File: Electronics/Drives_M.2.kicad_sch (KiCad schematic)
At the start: 87 parts, among them IC3 LM61480Q3RPHRQ1, J16 Bus_M.2_Socket_M, J17 Bus_M.2_Socket_M, J18 Bus_M.2_Socket_M, J19 Bus_M.2_Socket_M, M1 M.2 Screw, M10 M.2 Solder Nut, M11 M.2 Screw, M12 M.2 Screw, M13 M.2 Solder Nut, M14 M.2 Solder Nut, M15 M.2 Solder Nut, M16 M.2 Solder Nut, M17 M.2 Solder Nut, M18 M.2 Solder Nut, M19 M.2 Solder Nut, M2 M.2 Screw, M20 M.2 Solder Nut, M3 M.2 Solder Nut, M4 M.2 Solder Nut, M5 M.2 Solder Nut, M6 M.2 Solder Nut, M7 M.2 Solder Nut, M8 M.2 Solder Nut, M9 M.2 Solder Nut, U7 ASEK-32.768KHZ-L-R-T, U8 ASM1184

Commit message: Changed sata port
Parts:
- C58: renamed from C54; footprint Capacitor_SMD:C_0603_1608Metric -> Capacitor_SMD:C_0402_1005Metric
- C59: renamed from C55; footprint Capacitor_SMD:C_0603_1608Metric -> Capacitor_SMD:C_0402_1005Metric
- C60: renamed from C56; footprint Capacitor_SMD:C_0603_1608Metric -> Capacitor_SMD:C_0402_1005Metric
- C61: renamed from C57; footprint Capacitor_SMD:C_0603_1608Metric -> Capacitor_SMD:C_0402_1005Metric
- C62: renamed from C58; footprint Capacitor_SMD:C_0603_1608Metric -> Capacitor_SMD:C_0402_1005Metric
- C63: renamed from C59; footprint Capacitor_SMD:C_0603_1608Metric -> Capacitor_SMD:C_0402_1005Metric
- C69: renamed from C65; footprint Capacitor_SMD:C_0603_1608Metric -> Capacitor_SMD:C_0402_1005Metric
- C70: renamed from C66; footprint Capacitor_SMD:C_0603_1608Metric -> Capacitor_SMD:C_0402_1005Metric
- C71: renamed from C67; footprint Capacitor_SMD:C_0603_1608Metric -> Capacitor_SMD:C_0402_1005Metric
- C72: renamed from C68; footprint Capacitor_SMD:C_0603_1608Metric -> Capacitor_SMD:C_0402_1005Metric
- C73: renamed from C69; footprint Capacitor_SMD:C_0603_1608Metric -> Capacitor_SMD:C_0402_1005Metric
- C74: renamed from C70; footprint Capacitor_SMD:C_0603_1608Metric -> Capacitor_SMD:C_0402_1005Metric
- C82: renamed from C78; footprint Capacitor_SMD:C_0603_1608Metric -> Capacitor_SMD:C_0402_1005Metric
- C83: renamed from C79; footprint Capacitor_SMD:C_0603_1608Metric -> Capacitor_SMD:C_0402_1005Metric
- C84: renamed from C80; footprint Capacitor_SMD:C_0603_1608Metric -> Capacitor_SMD:C_0402_1005Metric
- C85: renamed from C81; footprint Capacitor_SMD:C_0603_1608Metric -> Capacitor_SMD:C_0402_1005Metric
- C86: renamed from C82; footprint Capacitor_SMD:C_0603_1608Metric -> Capacitor_SMD:C_0402_1005Metric
- C87: renamed from C83; footprint Capacitor_SMD:C_0603_1608Metric -> Capacitor_SMD:C_0402_1005Metric
- J16: renamed from J18; footprint M.2 M Key socket:M.2 M Key socket -> M.2 M Key socket:M.2 M Key socket WN HOLES
- J17: renamed from J19; footprint M.2 M Key socket:M.2 M Key socket -> M.2 M Key socket:M.2 M Key socket WN HOLES
- U8: footprint Package_DFN_QFN:QFN-64-1EP_9x9mm_P0.5mm_EP5.2x5.2mm -> Package_DFN_QFN:QFN-64-1EP_9x9mm_P0.5mm_EP5.2x5.2mm_ThermalVias
- renumbered C52 to C56, C53 to C57, C60 to C64, C61 to C65, C62 to C66, C63 to C67, C64 to C68, C71 to C75, C72 to C76, C73 to C77, C74 to C78, C75 to C79, C76 to C80, C77 to C81, C84 to C88, C85 to C89, C86 to C90, C87 to C91, C88 to C92, C89 to C93, J16 to J14, J17 to J15, R32 to R30, R33 to R31, R34 to R32, R35 to R33, R36 to R34, R37 to R35, R38 to R36, R39 to R37, R40 to R38, R41 to R39, R42 to R40, R43 to R41, R44 to R42, R45 to R43, R46 to R44, R47 to R45, TP12 to TP9

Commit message: More pcbing
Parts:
- removed TP9: TestPoint, TestPoint:TestPoint_Pad_1.0x1.0mm, symbol Connector:TestPoint
- added C94: 47u, Capacitor_SMD:C_0805_2012Metric, symbol Device:C_Small
- J16, J17: footprint M.2 M Key socket:M.2 M Key socket WN HOLES -> M.2 M Key socket:M.2 M Key socket
- R35: footprint Resistor_SMD:R_0603_1608Metric -> Resistor_SMD:R_0402_1005Metric
- renumbered C91 to C90, C92 to C91, C93 to C92, C90 to C93
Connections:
- net BOOT: now also IC3.16 (SW), L5.1
- net PCIe_CLK_N_3: now also J15.53 (REFCLKn)
- net PCIe_CLK_N_4: no longer J15.53 (REFCLKn)
- net PCIe_CLK_P_3: now also J15.55 (REFCLKp)
- net PCIe_CLK_P_4: no longer J15.55 (REFCLKp)
- net gnd: now also C94.2
- net TX_P_3: now reaches C67.2, U8.39 (TXP_3)
- net TX_N_3: now reaches C68.2, U8.40 (TXN_3)
- net FB renamed +3V3 M.2
- net +3V3 M.2: now also C94.1
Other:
- moved on the sheet: C67, C68, C91, C92, C93

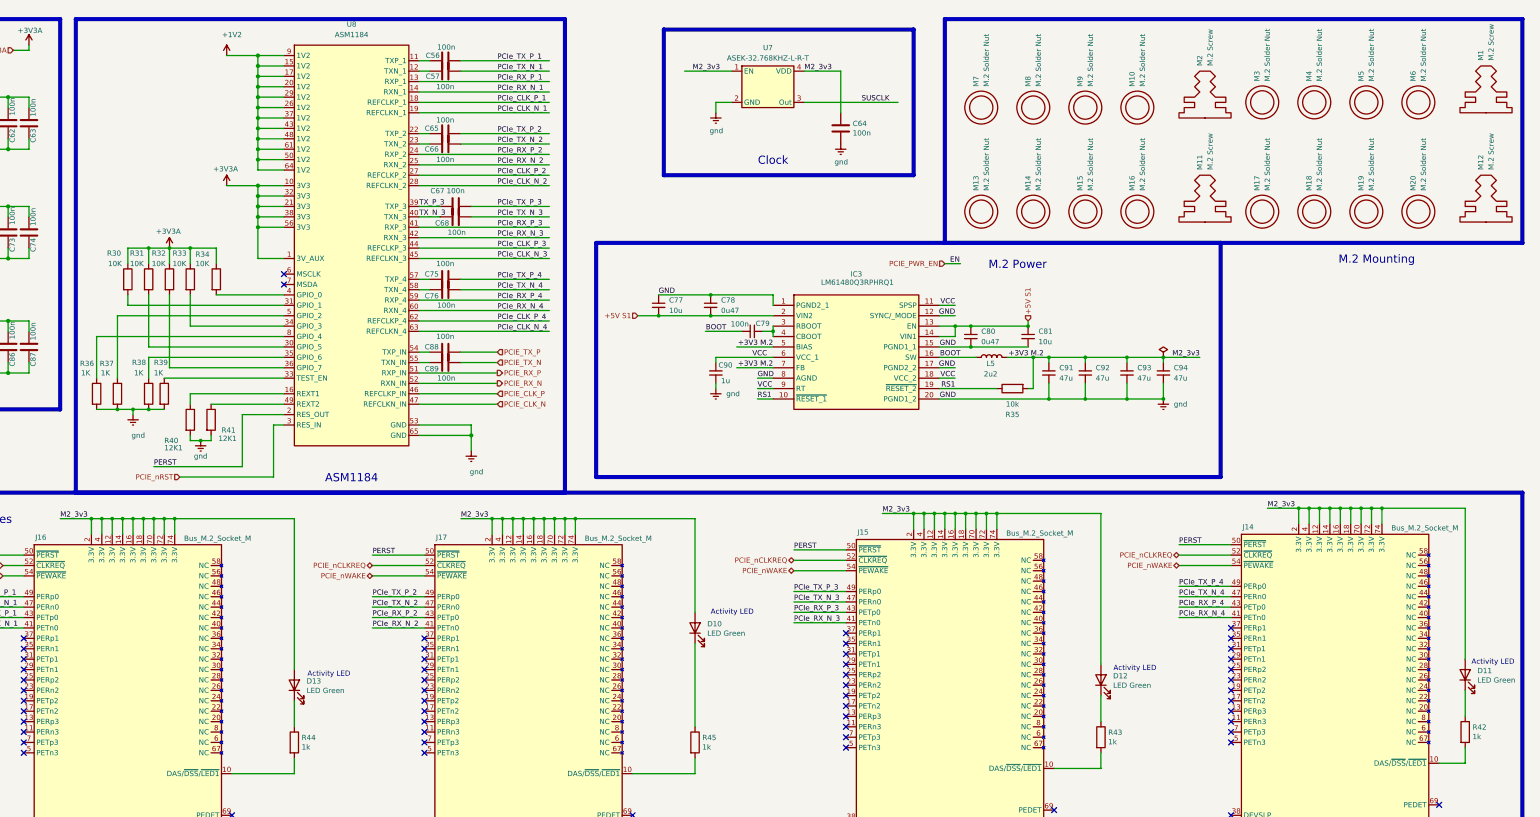
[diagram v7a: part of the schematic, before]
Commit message: More pcb arangment, verticle ports
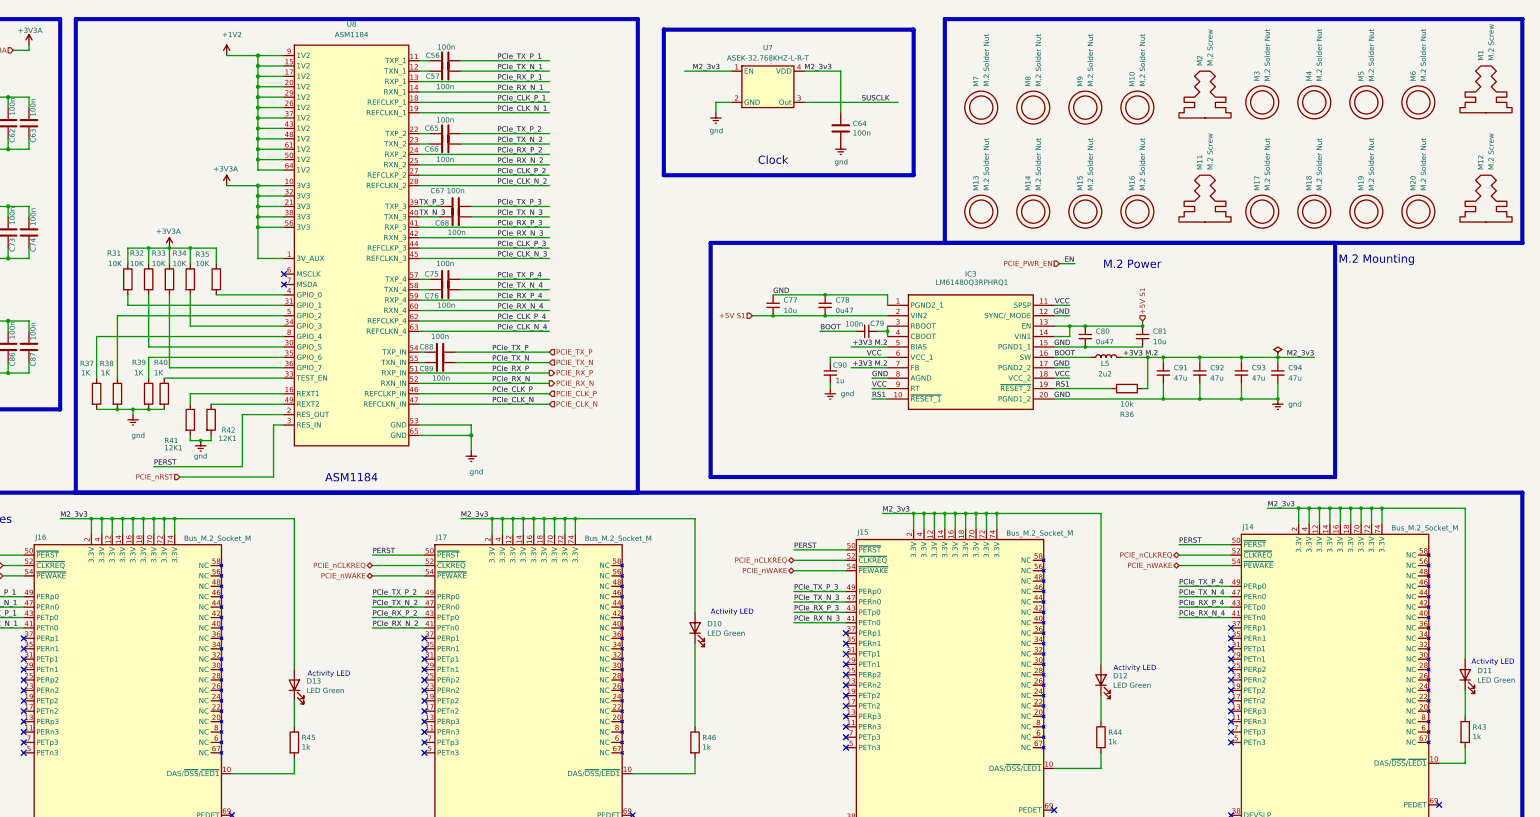
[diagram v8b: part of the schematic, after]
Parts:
- J14, J17: footprint M.2 M Key socket:M.2 M Key socket -> 2199119-5:21991195 no holes
- J15, J16: footprint M.2 M Key socket:M.2 M Key socket -> 2199119-5:21991195
- renumbered R30 to R31, R31 to R32, R32 to R33, R33 to R34, R34 to R35, R35 to R36, R36 to R37, R37 to R38, R38 to R39, R39 to R40, R40 to R41, R41 to R42, R42 to R43, R43 to R44, R44 to R45, R45 to R46
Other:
- moved on the sheet: C77, C78, C79, C80, C81, C88, C89, C90, C91, C92, C93, C94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
